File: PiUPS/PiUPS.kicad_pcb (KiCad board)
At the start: 2 copper layers, 87.4 x 56 mm, 92 parts, among them J1 USB_C_Receptacle_USB2.0, J2 Raspberry_Pi_2_3, J3 USB_A, J4 USB_B_Micro, J5 Screw_Terminal_01x02, J6 Screw_Terminal_01x02, Q1 IRF7404, Q2 IRF7404, Q3 IRLML2803TRPBF, Q4 IRF7404, Q5 IRF7404, Q6 IRLML2803TRPBF, Q7 IRLML2803TRPBF, SW1 MODE (JS102011SAQN), SW2 SW_MEC_5E, U1 LM358, U2 BQ25601, U3 TPS61088RHLR, U4 DS3231M

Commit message: beginning of routing
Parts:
- added C26: 100nF, Capacitor_SMD:C_0805_2012Metric_Pad1.18x1.45mm_HandSolder, F.Cu at (313.9, 46.2)
- added C8: 10uF, Capacitor_SMD:C_1206_3216Metric_Pad1.33x1.80mm_HandSolder, F.Cu at (94.2, 109.8)
- added D5: BZV55-B2V4.115, Diode_SMD:D_1206_3216Metric_Pad1.42x1.75mm_HandSolder, F.Cu at (269.0, 84.5)
- added D6: 1PS76SB40.115, Diode_SMD:D_SOD-323_HandSoldering, F.Cu at (268.1, 91.2)
- added Q8: IRF7404, Package_SO:SOIC-8_3.9x4.9mm_P1.27mm, F.Cu at (294.9, 47.9)
- added Q9: IRF7404, Package_SO:SOIC-8_3.9x4.9mm_P1.27mm, F.Cu at (252.2, 104.7)
- added R40: 470, Resistor_SMD:R_0805_2012Metric_Pad1.20x1.40mm_HandSolder, F.Cu at (318.6, 46.2)
- added R41: 470, Resistor_SMD:R_0805_2012Metric_Pad1.20x1.40mm_HandSolder, F.Cu at (250.3, 115.3)
- added R42: 10k, Resistor_SMD:R_0805_2012Metric_Pad1.20x1.40mm_HandSolder, F.Cu at (298.8, 69.4)
- added R43: 0, Resistor_SMD:R_0805_2012Metric_Pad1.20x1.40mm_HandSolder, F.Cu at (250.3, 118.3)
- added R44: 10k, Resistor_SMD:R_0805_2012Metric_Pad1.20x1.40mm_HandSolder, F.Cu at (312.3, 54.1)
- added R45: 470, Resistor_SMD:R_0805_2012Metric_Pad1.20x1.40mm_HandSolder, F.Cu at (306.5, 60.0)
- added R46: 470, Resistor_SMD:R_0805_2012Metric_Pad1.20x1.40mm_HandSolder, F.Cu at (298.8, 66.5)
- added R47: 10k, Resistor_SMD:R_0805_2012Metric_Pad1.20x1.40mm_HandSolder, F.Cu at (270.3, 97.1)
- added R48: 10k, Resistor_SMD:R_0805_2012Metric_Pad1.20x1.40mm_HandSolder, F.Cu at (293.0, 72.4)
- added R49: 10k, Resistor_SMD:R_0805_2012Metric_Pad1.20x1.40mm_HandSolder, F.Cu at (271.5, 94.1)
- added RT1: 10k, Resistor_SMD:R_0603_1608Metric, F.Cu at (110.1, 85.3)
- added U5: FS8205A, Package_SO:TSSOP-8_4.4x3mm_P0.65mm, F.Cu at (252.7, 63.8)
- added U6: DS3231M, Package_SO:SOIC-16W_7.5x10.3mm_P1.27mm, F.Cu at (180.2, 133.0)
- C1: value 47nF -> 20uF; footprint Capacitor_SMD:C_0805_2012Metric_Pad1.18x1.45mm_HandSolder -> Capacitor_SMD:C_1206_3216Metric_Pad1.33x1.80mm_HandSolder
- C10, C19, C24: value 100nF -> 10uF; footprint Capacitor_SMD:C_0805_2012Metric_Pad1.18x1.45mm_HandSolder -> Capacitor_SMD:C_1206_3216Metric_Pad1.33x1.80mm_HandSolder
- C11: value 20uF -> 47nF; footprint Capacitor_SMD:C_1206_3216Metric_Pad1.33x1.80mm_HandSolder -> Capacitor_SMD:C_0805_2012Metric_Pad1.18x1.45mm_HandSolder
- C12, C25, C3: value 10uF -> 100nF; footprint Capacitor_SMD:C_1206_3216Metric_Pad1.33x1.80mm_HandSolder -> Capacitor_SMD:C_0805_2012Metric_Pad1.18x1.45mm_HandSolder
- C13, C15: value 10uF -> 47uF; footprint Capacitor_SMD:C_1206_3216Metric_Pad1.33x1.80mm_HandSolder -> Capacitor_SMD:C_1210_3225Metric_Pad1.33x2.70mm_HandSolder
- C14: value 43pF -> 10uF; footprint Capacitor_SMD:C_0805_2012Metric_Pad1.18x1.45mm_HandSolder -> Capacitor_SMD:C_1206_3216Metric_Pad1.33x1.80mm_HandSolder
- C16: value 8.2nF -> 43pF
- C17: value 1nF -> 47uF; footprint Capacitor_SMD:C_0805_2012Metric_Pad1.18x1.45mm_HandSolder -> Capacitor_SMD:C_1210_3225Metric_Pad1.33x2.70mm_HandSolder
- C18: value 10uF -> 1nF; footprint Capacitor_SMD:C_1206_3216Metric_Pad1.33x1.80mm_HandSolder -> Capacitor_SMD:C_0805_2012Metric_Pad1.18x1.45mm_HandSolder
- C20: value 100nF -> 1000uF; footprint Capacitor_SMD:C_0805_2012Metric_Pad1.18x1.45mm_HandSolder -> Capacitor_SMD:CP_Elec_10x10; moved to F.Cu
- C21: footprint Capacitor_SMD:CP_Elec_10x10 -> Capacitor_SMD:CP_Elec_6.3x7.7
- C23: value 220uF -> 100nF; footprint Capacitor_SMD:CP_Elec_6.3x7.7 -> Capacitor_SMD:C_0805_2012Metric_Pad1.18x1.45mm_HandSolder
- C4: value 10uF -> 20uF
- C5: value 47uF -> 47nF; footprint Capacitor_SMD:C_1210_3225Metric_Pad1.33x2.70mm_HandSolder -> Capacitor_SMD:C_0805_2012Metric_Pad1.18x1.45mm_HandSolder
- C6: value 47uF -> 10uF; footprint Capacitor_SMD:C_1210_3225Metric_Pad1.33x2.70mm_HandSolder -> Capacitor_SMD:C_1206_3216Metric_Pad1.33x1.80mm_HandSolder
- C7: value 47uF -> 100nF; footprint Capacitor_SMD:C_1210_3225Metric_Pad1.33x2.70mm_HandSolder -> Capacitor_SMD:C_0805_2012Metric_Pad1.18x1.45mm_HandSolder
- C9: value 20uF -> 10uF
- D1: value BZV55-B2V4.115 -> 1PS76SB40.115; footprint Diode_SMD:D_1206_3216Metric_Pad1.42x1.75mm_HandSolder -> Diode_SMD:D_SOD-323_HandSoldering; moved to F.Cu
- D2: footprint LED_SMD:LED_0805_2012Metric -> LED_SMD:LED_1206_3216Metric_Pad1.42x1.75mm_HandSolder
- D3: value LED_G -> 1PS76SB40.115; footprint LED_SMD:LED_0805_2012Metric -> Diode_SMD:D_SOD-323_HandSoldering
- D4: value 1N4001 -> 1PS76SB40.115; footprint Diode_SMD:D_1206_3216Metric_Pad1.42x1.75mm_HandSolder -> Diode_SMD:D_SOD-323_HandSoldering; moved to F.Cu
- F1, Q2, Q3, Q4, Q7, R29, R35, R39: moved to F.Cu
- J2: value Raspberry_Pi_2_3 -> USB_B_Micro; footprint RPI:raspberrypi_2_3 -> Connector_USB:USB_Micro-B_Amphenol_10103594-0001LF_Horizontal
- J3: value USB_A -> Screw_Terminal_01x02; footprint Connector_USB:USB_A_Stewart_SS-52100-001_Horizontal -> TerminalBlock:TerminalBlock_Altech_AK300-2_P5.00mm
- J4: value USB_B_Micro -> USB_A; footprint Connector_USB:USB_Micro-B_GCT_USB3076-30-A -> USB:SAMTEC_USB-A-S-X-X-SM2
- J6: value Screw_Terminal_01x02 -> Raspberry_Pi_2_3; footprint TerminalBlock:TerminalBlock_Altech_AK300-2_P5.00mm -> RPI:raspberrypi_2_3
- L2: footprint Inductor_SMD:L_10.4x10.4_H4.8 -> Inductor_SMD:L_6.3x6.3_H3
- Q1, Q5: value IRF7404 -> IRLML2803TRPBF; footprint Package_SO:SOIC-8_3.9x4.9mm_P1.27mm -> IRLML2803TRPBF:SOT95P237X112-3N; moved to F.Cu
- Q6: value IRLML2803TRPBF -> IRF7404; footprint IRLML2803TRPBF:SOT95P237X112-3N -> Package_SO:SOIC-8_3.9x4.9mm_P1.27mm; moved to F.Cu
- R1: value 64.9k -> 10k
- R10: value 10k -> 5.1k; moved to F.Cu
- R11: value 5.1k -> 470
- R12: value 0 -> 470; moved to F.Cu
- R13: value 5.1k -> 10k
- R14: value 100 -> 18k; moved to F.Cu
- R15: value 5.1k -> 200k
- R16: value USR -> 174k
- R17: value USR -> 10k; moved to F.Cu
- R19: value USR -> 1k
- R2, R3, R36, R4: value 10k -> 470; moved to F.Cu
- R20: value USR -> 64.9k
- R21: value USR -> 210k
- R22: value 10k -> 147k; moved to F.Cu
- R23: value 470 -> 100; moved to F.Cu
- R24: value 18.7k -> 470
- R25: value 174k -> 18.7k
- R26: value USR -> 470
- R27: value 147k -> 470
- R28, R31, R33: value 10k -> USR
- R30, R34, R6: value 10k -> USR; moved to F.Cu
- R32: value USR -> 10k
- R37, R38: value 470 -> 10k; moved to F.Cu
- R5: value 210k -> 10k
- R7: value 1k -> 5.1k; moved to F.Cu
- R8: value 1k -> 10k; moved to F.Cu
- SW1: value MODE (JS102011SAQN) -> SW_MEC_5E; footprint Button_Switch_SMD:SW_SPDT_CK-JS102011SAQN -> Button_Switch_SMD:SW_SPST_Omron_B3FS-100xP; moved to F.Cu
- SW2: value SW_MEC_5E -> MODE (JS102011SAQN); footprint Button_Switch_SMD:SW_SPST_Omron_B3FS-100xP -> Button_Switch_SMD:SW_SPDT_CK-JS102011SAQN
- U1: value LM358 -> LM393; moved to F.Cu
- U2: value BQ25601 -> BQ25895RTW
- U4: value DS3231M -> DW01; footprint Package_SO:SOIC-16W_7.5x10.3mm_P1.27mm -> Package_TO_SOT_SMD:SOT-23-6; moved to F.Cu
- moved R15 237.4 mm to (312.8, 49.5), turned to 0 degrees
- moved R32 236.9 mm to (306.1, 63.0), turned to 0 degrees
- moved R14 234.9 mm to (307.5, 54.1)
- moved R28 233.2 mm to (317.5, 52.1), turned to 0 degrees
- moved Q1 226.4 mm to (301.6, 56.7), turned to 0 degrees
- moved D1 225.1 mm to (296.4, 63.5), turned to 0 degrees
- moved R13 222.8 mm to (301.4, 60.4), turned to 0 degrees
- moved R30 222.7 mm to (292.9, 75.3), turned to 0 degrees
- moved R29 215.6 mm to (284.0, 84.6), turned to 0 degrees
- moved U1 215.3 mm to (282.3, 61.9), turned to 0 degrees
- moved Q7 213.8 mm to (307.9, 50.3), turned to 0 degrees
- moved C4 211.9 mm to (282.7, 71.1), turned to 0 degrees
- moved R2 209.4 mm to (279.3, 81.7)
- moved R11 206.3 mm to (283.4, 78.7)
- moved R26 206.1 mm to (311.2, 57.1), turned to 0 degrees
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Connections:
- C1 pad 2: Net-(C1-Pad2) -> GND
- C10 pad 2: GND -> GND1
- C11 pad 1: Net-(C10-Pad1) -> Net-(C11-Pad1)
- C13 pad 1: +BATT -> GND
- C13 pad 2: GND -> VOUT
- C15 pad 1: Net-(C15-Pad1) -> GND
- C15 pad 2: GND -> VOUT
- C17 pad 1: Net-(C17-Pad1) -> GND
- C17 pad 2: GND -> VOUT
- C18 pad 1: GND -> Net-(C18-Pad1)
- C18 pad 2: Net-(C18-Pad2) -> GND
- C19 pad 1: Net-(C19-Pad1) -> +BATT
- C19 pad 2: Net-(C19-Pad2) -> GND
- C2 pad 1: VSYS -> +5V
- C20 pad 1: Net-(C20-Pad1) -> V_UPS
- C20 pad 2: Net-(C20-Pad2) -> GND
- C25 pad 1: V_UPS -> Net-(C25-Pad1)
- C25 pad 2: GND -> Net-(C25-Pad2)
- C3 pad 1: VSYS -> Net-(C1-Pad1)
- C4 pad 1: +5V -> Net-(C1-Pad1)
- C5 pad 1: GND -> Net-(C5-Pad1)
- C5 pad 2: VOUT -> Net-(C5-Pad2)
- C6 pad 1: GND -> GND1
- C6 pad 2: VOUT -> Net-(C6-Pad2)
- C7 pad 1: GND -> Net-(C7-Pad1)
- C7 pad 2: VOUT -> Net-(C7-Pad2)
- C9 pad 1: Net-(C10-Pad1) -> VSYS
- C9 pad 2: GND -> GND1
- D1 pad 2: GND -> +5V
- D2 pad 2: VSYS -> Net-(D2-Pad2)
- D3 pad 2: VSYS -> Net-(D3-Pad2)
- D4 pad 2: +BATT -> Net-(D3-Pad2)
- F1 pad 1: Net-(C10-Pad1) -> Net-(F1-Pad1)
- F2 pad 1: Net-(C10-Pad1) -> Net-(F1-Pad1)
- J1 pad A6: Net-(J1-PadA6) -> unconnected-(J1-PadA6)
- J1 pad A7: Net-(J1-PadA7) -> unconnected-(J1-PadA7)
- J1 pad A8: Net-(J1-PadA8) -> unconnected-(J1-PadA8)
- J1 pad B6: Net-(J1-PadB6) -> unconnected-(J1-PadB6)
- J1 pad B7: Net-(J1-PadB7) -> unconnected-(J1-PadB7)
- J1 pad B8: Net-(J1-PadB8) -> unconnected-(J1-PadB8)
- J2 pad 1: Pi_3v3 -> +5V
- J2 pad 2: V_UPS -> Net-(J2-Pad2)
- J2 pad 3: SDA -> Net-(J2-Pad3)
- J2 pad 4: V_UPS -> unconnected-(J2-Pad4)
- J2 pad 5: SCL -> GND
- J3 pad 1: Net-(F3-Pad2) -> +BATT
- J3 pad 2: Net-(J3-Pad2) -> GND
- J4 pad 1: +5V -> Net-(F3-Pad2)
- J4 pad 4: Net-(J4-Pad4) -> GND
- J6 pad 1: +BATT -> Pi_3v3
- J6 pad 2: GND -> V_UPS
- L1 pad 1: Net-(C1-Pad1) -> Net-(C7-Pad1)
- L1 pad 2: VSYS -> Net-(C1-Pad1)
- L2 pad 1: Net-(C19-Pad1) -> Net-(C5-Pad1)
- L2 pad 2: Net-(C10-Pad1) -> VSYS
- Q1 pad 2: Net-(Q1-Pad1) -> GND
- Q1 pad 3: Net-(Q1-Pad1) -> Net-(Q1-Pad3)
- Q2 pad 1: Net-(Q1-Pad1) -> Net-(F1-Pad1)
- Q2 pad 2: Net-(Q1-Pad1) -> Net-(F1-Pad1)
- Q2 pad 3: Net-(Q1-Pad1) -> Net-(F1-Pad1)
- Q2 pad 4: Net-(Q1-Pad4) -> Net-(Q1-Pad3)
- Q2 pad 5: V_UPS -> Net-(C1-Pad1)
- Q2 pad 6: V_UPS -> Net-(C1-Pad1)
- Q2 pad 7: V_UPS -> Net-(C1-Pad1)
- Q2 pad 8: V_UPS -> Net-(C1-Pad1)
- Q3 pad 1: Net-(Q3-Pad1) -> Net-(C25-Pad1)
- Q4 pad 1: Net-(C20-Pad1) -> Net-(Q4-Pad1)
- Q4 pad 2: Net-(C20-Pad1) -> Net-(Q4-Pad1)
- Q4 pad 3: Net-(C20-Pad1) -> Net-(Q4-Pad1)
- Q4 pad 4: Net-(C20-Pad2) -> Net-(Q4-Pad4)
- Q4 pad 5: VOUT -> +5V
- Q4 pad 6: VOUT -> +5V
- Q4 pad 7: VOUT -> +5V
- Q4 pad 8: VOUT -> +5V
- Q5 pad 1: Net-(C20-Pad1) -> Net-(Q5-Pad1)
- Q5 pad 2: Net-(C20-Pad1) -> GND
- Q5 pad 3: Net-(C20-Pad1) -> Net-(Q5-Pad3)
- Q6 pad 1: Net-(Q6-Pad1) -> Net-(C26-Pad1)
- Q6 pad 2: GND -> Net-(C26-Pad1)
- Q6 pad 3: Net-(Q6-Pad3) -> Net-(C26-Pad1)
- R1 pad 1: Net-(R1-Pad1) -> GND
- R1 pad 2: GND -> Net-(R1-Pad2)
- R10 pad 1: INT -> Net-(J1-PadA5)
- R10 pad 2: Pi_3v3 -> GND
- R11 pad 1: Net-(J1-PadB5) -> Net-(R11-Pad1)
- R11 pad 2: GND -> Net-(R11-Pad2)
- R12 pad 1: Net-(J2-Pad7) -> Net-(R11-Pad2)
- R12 pad 2: INT -> GND1
- R13 pad 1: Net-(D2-Pad1) -> GND1
- R14 pad 1: Net-(Q3-Pad3) -> Net-(R14-Pad1)
- R14 pad 2: Net-(Q1-Pad4) -> Net-(C1-Pad1)
- R15 pad 1: Net-(D3-Pad1) -> GND
- R15 pad 2: Net-(R15-Pad2) -> Net-(R14-Pad1)
- R16 pad 1: Net-(J3-Pad3) -> Net-(C7-Pad1)
- R16 pad 2: V_UPS -> Net-(R16-Pad2)
- R17 pad 1: Net-(D4-Pad1) -> Net-(R17-Pad1)
- R17 pad 2: +BATT -> Net-(C6-Pad2)
- R18 pad 1: Net-(R18-Pad1) -> GND1
- R18 pad 2: GND -> Net-(R17-Pad1)
- R19 pad 1: GND -> GND1
- R19 pad 2: Net-(J3-Pad3) -> Net-(R19-Pad2)
- R2 pad 2: +5V -> Net-(R2-Pad2)
- R20 pad 1: Net-(J3-Pad3) -> Net-(R20-Pad1)
- R20 pad 2: Net-(J3-Pad2) -> GND
- R21 pad 1: Net-(J3-Pad2) -> VOUT
- R21 pad 2: V_UPS -> Net-(R20-Pad1)
- R22 pad 1: Net-(R22-Pad1) -> GND
- R22 pad 2: VSYS -> Net-(R22-Pad2)
- R23 pad 1: Net-(R23-Pad1) -> +BATT
- R23 pad 2: Net-(Q3-Pad1) -> Net-(C12-Pad1)
- R24 pad 1: Net-(C17-Pad1) -> Net-(D3-Pad2)
- R24 pad 2: Net-(C14-Pad1) -> +5V
- R25 pad 1: Net-(C19-Pad1) -> Net-(C18-Pad1)
- R25 pad 2: Net-(R25-Pad2) -> Net-(C16-Pad1)
- R26 pad 1: GND -> 2V4
- R26 pad 2: Net-(J3-Pad2) -> VOUT
- R27 pad 1: GND -> 2V4
- R27 pad 2: Net-(R27-Pad2) -> VOUT
- R28 pad 1: Net-(R28-Pad1) -> Net-(J4-Pad3)
- R28 pad 2: Net-(C15-Pad1) -> Net-(J4-Pad2)
- R29 pad 1: GND -> Net-(C25-Pad2)
- R29 pad 2: Net-(R22-Pad1) -> GND
- R3 pad 1: Net-(R2-Pad1) -> Net-(D1-Pad1)
- R3 pad 2: GND -> Net-(R2-Pad1)
- R30 pad 1: Net-(Q3-Pad1) -> Net-(J4-Pad3)
- R30 pad 2: GND -> V_UPS
- R31 pad 2: Net-(R28-Pad1) -> Net-(J4-Pad2)
- R32 pad 1: Net-(J4-Pad3) -> Net-(C25-Pad2)
- R32 pad 2: Net-(J4-Pad2) -> +5V
- R33 pad 1: Net-(R33-Pad1) -> GND
- R33 pad 2: VSYS -> Net-(J4-Pad3)
- R34 pad 1: Net-(C20-Pad2) -> Net-(J4-Pad2)
- R34 pad 2: Net-(C20-Pad1) -> V_UPS
- R35 pad 1: Net-(Q6-Pad3) -> Net-(R35-Pad1)
- R35 pad 2: Net-(C20-Pad2) -> VOUT
- R36 pad 1: Net-(Q6-Pad1) -> Net-(R35-Pad1)
- R36 pad 2: VOUT -> Net-(C25-Pad1)
- R37 pad 1: Net-(Q7-Pad3) -> GND
- R37 pad 2: Net-(Q6-Pad1) -> Net-(C25-Pad1)
- R38 pad 1: Net-(R23-Pad1) -> Net-(Q7-Pad1)
- R38 pad 2: Net-(Q7-Pad1) -> VOUT
- R39 pad 1: GND -> SDA
- R39 pad 2: Net-(Q7-Pad1) -> Pi_3v3
- R4 pad 1: SDA -> Net-(R4-Pad1)
- R4 pad 2: Pi_3v3 -> Net-(R2-Pad1)
- R5 pad 1: VOUT -> Net-(F1-Pad1)
- R5 pad 2: Net-(R1-Pad1) -> Net-(Q1-Pad3)
- R6 pad 1: SCL -> Net-(J2-Pad3)
- R6 pad 2: Pi_3v3 -> Net-(J2-Pad2)
- R7 pad 1: Net-(D1-Pad1) -> Net-(J1-PadB5)
- R7 pad 2: VSYS -> GND
- R8 pad 1: Net-(Q1-Pad4) -> Net-(R2-Pad1)
- R8 pad 2: Net-(Q1-Pad1) -> Net-(C1-Pad1)
- R9 pad 1: Net-(J1-PadA5) -> VSYS
- R9 pad 2: GND -> Net-(D2-Pad2)
- SW1 pad 1: VSYS -> +BATT
- SW1 pad 2: Net-(SW1-Pad2) -> +BATT
- SW1 pad 3: GND -> Net-(R2-Pad2)
- SW2 pad 1: GND -> Net-(R2-Pad1)
- SW2 pad 2: GND -> Net-(Q1-Pad1)
- SW2 pad 3: Net-(SW2-Pad3) -> Net-(R1-Pad2)
- U1 pad 1: Net-(R23-Pad1) -> Net-(R35-Pad1)
- U1 pad 2: Net-(D1-Pad1) -> 2V4
- U1 pad 3: Net-(R2-Pad1) -> Net-(C25-Pad2)
- U1 pad 5: Net-(R22-Pad1) -> Net-(R14-Pad1)
- U1 pad 6: Net-(U1-Pad6) -> 2V4
- U1 pad 7: Net-(U1-Pad6) -> Net-(R4-Pad1)
- U1 pad 8: VSYS -> VOUT
- U2 pad 10: Net-(U2-Pad10) -> Net-(R11-Pad1)
- U2 pad 11: Net-(R28-Pad1) -> Net-(R17-Pad1)
- U2 pad 12: Net-(SW2-Pad3) -> unconnected-(U2-Pad12)
- U2 pad 17: GND -> GND1
- U2 pad 18: GND -> GND1
- U2 pad 19: Net-(C1-Pad1) -> Net-(C5-Pad1)
- U2 pad 2: Net-(R33-Pad1) -> Net-(U2-Pad2)
- U2 pad 20: Net-(C1-Pad1) -> Net-(C5-Pad1)
- U2 pad 21: Net-(C1-Pad2) -> Net-(C5-Pad2)
- U2 pad 22: Net-(C15-Pad1) -> Net-(C6-Pad2)
- U2 pad 23: Net-(C18-Pad2) -> Net-(C10-Pad1)
- U2 pad 24: +5V -> unconnected-(U2-Pad24)
- U2 pad 25: GND -> GND1
- U2 pad 3: Net-(R15-Pad2) -> Net-(U2-Pad2)
- U2 pad 4: Net-(R13-Pad2) -> Net-(D2-Pad1)
- U2 pad 8: Net-(U2-Pad8) -> GND1
- U2 pad 9: Net-(R18-Pad1) -> Net-(R13-Pad2)
- U3 pad 1: Net-(C12-Pad1) -> Net-(C14-Pad1)
- U3 pad 10: Net-(C16-Pad1) -> Net-(C11-Pad1)
- U3 pad 11: GND -> unconnected-(U3-Pad11)
- U3 pad 12: GND -> unconnected-(U3-Pad12)
- U3 pad 13: Net-(U3-Pad13) -> unconnected-(U3-Pad13)
- U3 pad 17: Net-(R1-Pad1) -> Net-(R20-Pad1)
- U3 pad 18: Net-(C14-Pad1) -> Net-(C16-Pad1)
- U3 pad 19: Net-(R27-Pad2) -> Net-(R22-Pad2)
- U3 pad 2: Net-(SW1-Pad2) -> VSYS
- U3 pad 3: Net-(R25-Pad2) -> Net-(R16-Pad2)
- U3 pad 4: Net-(C19-Pad1) -> Net-(C7-Pad1)
- U3 pad 5: Net-(C19-Pad1) -> Net-(C7-Pad1)
- U3 pad 6: Net-(C19-Pad1) -> Net-(C7-Pad1)
- U3 pad 7: Net-(C19-Pad1) -> Net-(C7-Pad1)
- U3 pad 8: Net-(C19-Pad2) -> Net-(C7-Pad2)
- U3 pad 9: Net-(C10-Pad1) -> Net-(C1-Pad1)
- U4 pad 1: Net-(U4-Pad1) -> Net-(D4-Pad1)
- U4 pad 2: Pi_3v3 -> Net-(R19-Pad2)
- U4 pad 3: Net-(U4-Pad3) -> Net-(D3-Pad1)
- U4 pad 4: Net-(U4-Pad4) -> unconnected-(U4-Pad4)
- U4 pad 5: GND -> Net-(C12-Pad1)
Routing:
- net VSYS: track 113.8 -> 0.00 mm, vias 3 -> 0
- net SDA: track 114.6 -> 1.52 mm, vias 3 -> 1
- net Net-(R23-Pad1): track 105.5 -> 0.00 mm, vias 4 -> 0
- net SCL: track 104.3 -> 1.86 mm, vias 3 -> 1
- net V_UPS: track 95.2 -> 0.00 mm, vias 48 -> 0
- net INT: track 89.3 -> 1.47 mm, vias 3 -> 1
- net Pi_3v3: track 72.8 -> 0.00 mm, vias 2 -> 0
- net GND: track 67.2 -> 0.00 mm, vias 19 -> 0
- net Net-(SW2-Pad3): track 47.6 -> 0.00 mm, vias 2 -> 0
- net Net-(SW1-Pad2): track 35.1 -> 0.00 mm, vias 1 -> 0
- net Net-(C15-Pad1): track 35.1 -> 0.00 mm, vias 2 -> 0
- net Net-(R33-Pad1): track 21.6 -> 0.00 mm
- net +BATT: track 17.0 -> 0.00 mm, vias 20 -> 0
- net VOUT: track 16.6 -> 0.00 mm, vias 9 -> 0
- net +5V: track 37.0 -> 22.2 mm, vias 6 -> 0
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- added copper zone on F.Cu, net Net-(C5-Pad1)
- removed copper zone on B.Cu, net +5V
- removed copper zone on F.Cu, net +5V
- removed copper zone on B.Cu, net +BATT
- removed copper zone on F.Cu, net +BATT
- removed copper zone on B.Cu, net GND
- removed copper zone on F.Cu, net GND
- removed copper zone on F.Cu, net Net-(C1-Pad1)
- removed copper zone on B.Cu, net Net-(C10-Pad1)
- removed copper zone on F.Cu, net Net-(C10-Pad1)
- removed copper zone on F.Cu, net Net-(C19-Pad1)
- removed copper zone on B.Cu, net Net-(C20-Pad1)
- removed copper zone on B.Cu, net Net-(Q1-Pad1)
- removed copper zone on B.Cu, net VOUT
- removed copper zone on F.Cu, net VOUT
- removed copper zone on F.Cu, net VSYS
- removed copper zone on B.Cu, net V_UPS
- removed copper zone on F.Cu, net V_UPS
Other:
- board text removed: "+"
- board text removed: "18650 BATT"
- board text removed: "5VIN"
- board text removed: "BAT EN"
- board text removed: "DDL PI UPS rev 0.2"
- board text removed: "EXT BATT"
- board text removed: "OUTDATED PCB"
- board text removed: "Place a shunt or a diode to enable RTC (see RTC notes)"
- board text removed: "Place a shunt to enable interrupt from battery management chip"
- board text removed: "Select USB port or screw terminal"
- board text removed: "Select resistors to suit your load (see USB notes)"
- board text removed: "UPS OFF ON"
- board text removed: "UPS VOUT"
- board text removed: "dmytroengineering.com/piups"

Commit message: Continued routing
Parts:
- C8: value 10uF -> 100nF; footprint Capacitor_SMD:C_1206_3216Metric_Pad1.33x1.80mm_HandSolder -> Capacitor_SMD:C_0805_2012Metric_Pad1.18x1.45mm_HandSolder
- R21: renamed from R6; moved to B.Cu
- R6: renamed from R10; moved to B.Cu
- R7: moved to B.Cu
- moved R21 252.1 mm to (73.3, 111.6), turned to 90 degrees
- moved R18 222.5 mm to (86.1, 116.9), turned to 180 degrees
- moved R9 200.6 mm to (86.1, 115.0)
- moved U3 196.7 mm to (107.7, 115.4)
- moved R6 187.0 mm to (77.5, 120.1), turned to -90 degrees
- moved R7 178.8 mm to (80.5, 120.2), turned to -90 degrees
- moved R12 161.3 mm to (89.0, 115.9), turned to -90 degrees
- moved U4 161.3 mm to (101.4, 119.8)
- moved C8 22.4 mm to (116.3, 106.5)
- moved R14 6.26 mm to (91.4, 118.0)
- moved C3 5.56 mm to (92.9, 105.4), turned to 90 degrees
- moved R19 3.53 mm to (88.5, 118.9)
- renumbered C2 to C1, C15 to C10, C17 to C11, C20 to C12, C21 to C13, C22 to C14, C23 to C15, C24 to C16, C25 to C17, C1 to C18, C3 to C19, C5 to C2, C4 to C20, C14 to C21, C16 to C22, C11 to C23, C18 to C24, C7 to C25, C9 to C3, C10 to C4, C12 to C5, C19 to C6, C6 to C7, C26 to C8, C13 to C9, D5 to D1, D3 to D2, D4 to D3, D2 to D4, D1 to D5, J6 to J4, J4 to J5, J5 to J6, L2 to L1, L1 to L2, Q4 to Q1, Q8 to Q2, Q5 to Q3, Q6 to Q4, Q9 to Q5, Q7 to Q6, Q3 to Q7, Q2 to Q8, Q1 to Q9, R32 to R1, R45 to R10, R23 to R11, R41 to R13, R17 to R14, R19 to R15, R24 to R16, R9 to R17, R13 to R18, R18 to R19, R29 to R2, R44 to R20, R49 to R22, R46 to R23, R38 to R24, R40 to R25, R20 to R26, R36 to R27, R21 to R28, R37 to R29, R26 to R3, R5 to R30, R1 to R31, R25 to R32, R16 to R33, R22 to R34, R2 to R35, R3 to R36, R8 to R37, R4 to R38, R14 to R39, R27 to R4, R39 to R40, R15 to R41, R47 to R43, R43 to R44, R30 to R45, R33 to R46, R28 to R47, R34 to R48, R31 to R49, R48 to R5, R35 to R8, R11 to R9, U4 to U3, U5 to U4, U3 to U5
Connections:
- C8 pad 1: Net-(C26-Pad1) -> Net-(C8-Pad1)
- C8 pad 2: Net-(C26-Pad2) -> Net-(C8-Pad2)
- C8 pad 1: VSYS -> Net-(C8-Pad1)
- C8 pad 2: GND1 -> Net-(C8-Pad2)
- Q4 pad 1: Net-(C26-Pad1) -> Net-(C8-Pad1)
- Q4 pad 2: Net-(C26-Pad1) -> Net-(C8-Pad1)
- Q4 pad 3: Net-(C26-Pad1) -> Net-(C8-Pad1)
- Q4 pad 4: Net-(C26-Pad2) -> Net-(C8-Pad2)
- Q5 pad 1: Net-(C26-Pad1) -> Net-(C8-Pad1)
- Q5 pad 2: Net-(C26-Pad1) -> Net-(C8-Pad1)
- Q5 pad 3: Net-(C26-Pad1) -> Net-(C8-Pad1)
- Q5 pad 4: Net-(C26-Pad2) -> Net-(C8-Pad2)
- R22 pad 1: Net-(C26-Pad2) -> Net-(C8-Pad2)
- R22 pad 2: Net-(C26-Pad1) -> Net-(C8-Pad1)
- R23 pad 2: Net-(C26-Pad2) -> Net-(C8-Pad2)
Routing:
- net Net-(R14-Pad1): track 0.00 -> 59.7 mm, vias 0 -> 2
- net GND1: track 0.00 -> 26.3 mm
- net Net-(C7-Pad2): track 2.04 -> 24.1 mm, vias 0 -> 2
- net Net-(R18-Pad2): track 0.00 -> 6.12 mm
- net Net-(J2-Pad2): track 0.00 -> 5.90 mm, vias 0 -> 1
- net Net-(J2-Pad3): track 0.00 -> 5.51 mm, vias 0 -> 1
- net Net-(R9-Pad1): track 0.00 -> 4.69 mm
- net Net-(J1-PadA5): track 0.00 -> 2.67 mm, vias 0 -> 1
- net Net-(J1-PadB5): track 0.00 -> 2.59 mm, vias 0 -> 1
- net +5V: track 22.2 -> 24.0 mm
- net +BATT: vias 0 -> 6
- added copper zone on B.Cu, net +BATT
- added copper zone on F.Cu, net +BATT
- added copper zone on F.Cu, net GND1
- added copper zone on F.Cu, net VSYS

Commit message: continued routing
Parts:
- moved R16 217.9 mm to (95.7, 112.3), turned to 90 degrees
- moved R3 214.8 mm to (101.9, 105.1)
- moved R4 207.5 mm to (98.1, 105.1), turned to 180 degrees
- moved R15 204.8 mm to (95.6, 119.7), turned to -90 degrees
- moved D5 200.9 mm to (101.9, 113.7), turned to 180 degrees
- moved R8 193.0 mm to (95.2, 106.0), turned to 90 degrees
- moved R30 191.8 mm to (106.1, 104.6), turned to 180 degrees
- moved U1 187.9 mm to (100.4, 108.8)
- moved C5 183.7 mm to (98.8, 116.1), turned to 90 degrees
- moved R11 183.5 mm to (92.3, 122.2), turned to 180 degrees
- moved R38 181.3 mm to (100.8, 117.0), turned to -90 degrees
- moved F2 176.7 mm to (97.4, 102.0), turned to 180 degrees
- moved C20 175.7 mm to (109.2, 98.6), turned to 90 degrees
- moved R35 175.1 mm to (107.5, 115.7)
- moved C10 174.4 mm to (114.4, 113.2)
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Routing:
- net +5V: track 24.0 -> 61.4 mm, vias 0 -> 11
- net GND1: track 26.3 -> 57.5 mm, vias 0 -> 11
- net +BATT: track 0.00 -> 27.5 mm, vias 6 -> 8
- net VSYS: track 0.00 -> 26.6 mm, vias 0 -> 3
- net Net-(R13-Pad1): track 0.00 -> 22.7 mm
- net Net-(C18-Pad1): track 0.00 -> 18.5 mm, vias 0 -> 2
- net VOUT: track 0.00 -> 17.9 mm, vias 0 -> 2
- net Net-(D3-Pad1): track 0.00 -> 16.1 mm, vias 0 -> 2
- net Net-(D5-Pad1): track 0.00 -> 15.1 mm, vias 0 -> 2
- net 2V4: track 0.00 -> 14.7 mm
- net Net-(C5-Pad1): track 0.00 -> 12.9 mm, vias 0 -> 2
- net Net-(D2-Pad1): track 0.00 -> 10.2 mm
- net Net-(R35-Pad1): track 0.00 -> 9.92 mm
- net Net-(R38-Pad1): track 0.00 -> 9.81 mm, vias 0 -> 2
- net Net-(C25-Pad1): track 0.00 -> 9.32 mm
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- added copper zone on F.Cu, net +5V
- added copper zone on B.Cu, net GND1
- added copper zone on F.Cu, net Net-(C18-Pad1)
- added copper zone on F.Cu, net Net-(C25-Pad1)
- added copper zone on F.Cu, net Net-(F1-Pad1)
- added copper zone on F.Cu, net VOUT

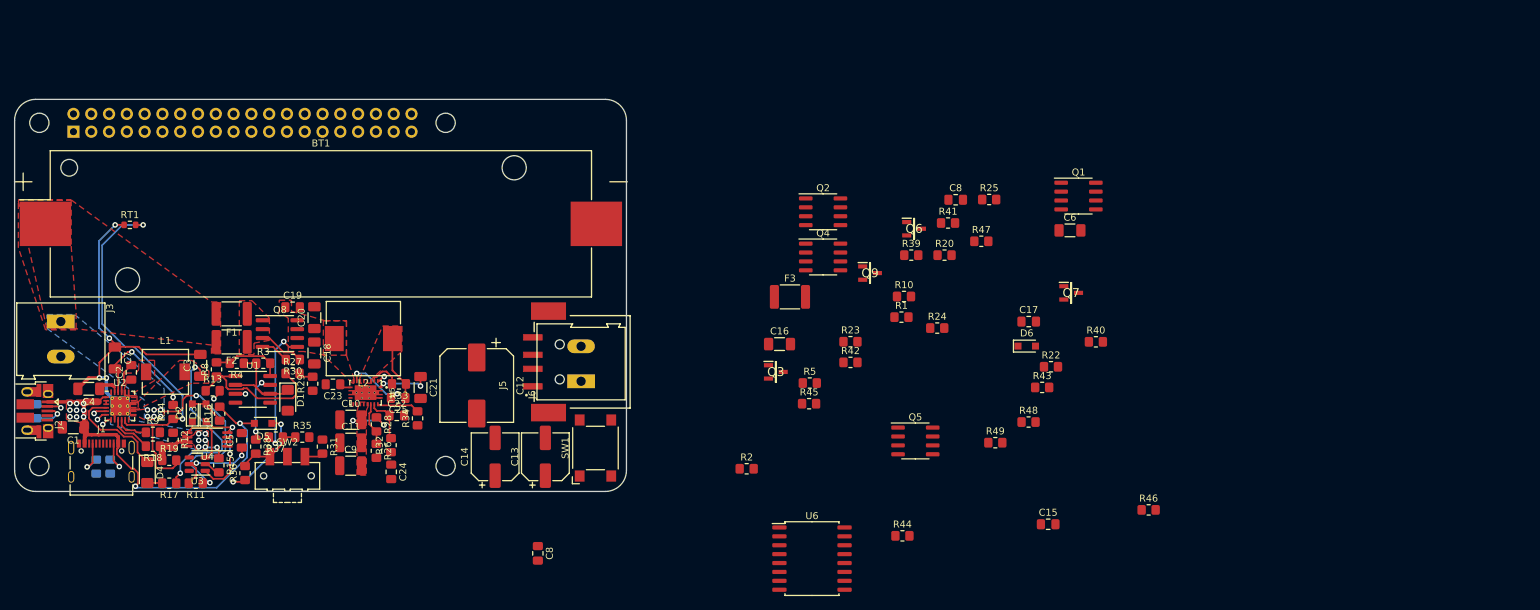
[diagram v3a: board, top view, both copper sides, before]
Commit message: almost finished routing
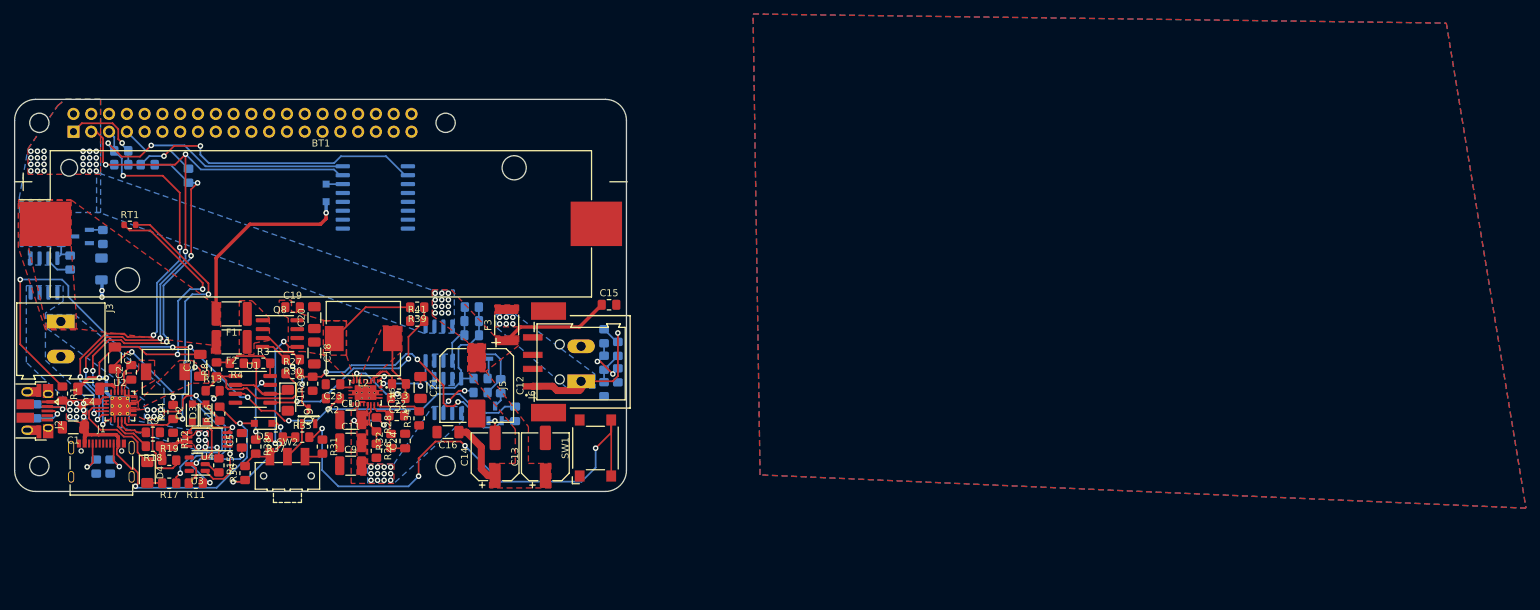
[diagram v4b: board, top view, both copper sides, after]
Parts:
- C17, C6, C8 (x2), D6, Q1, Q2, Q3, Q4, Q5, Q6, Q7, R10, R20, R22, R23, R24, R25, R40, R42, R43, R44, R45, R46, R47, R48, R49, R5, U6: moved to B.Cu
- moved Q1 148.1 mm to (70.6, 92.6), turned to -90 degrees
- moved R40 141.4 mm to (81.6, 76.8)
- moved C6 138.4 mm to (78.8, 91.6), turned to 90 degrees
- moved R43 131.6 mm to (85.4, 76.8), turned to 180 degrees
- moved R10 120.6 mm to (73.0, 86.9), turned to -90 degrees
- moved R1 120.3 mm to (73.2, 109.4), turned to -90 degrees
- moved R20 120.2 mm to (79.0, 87.1), turned to -90 degrees
- moved R44 114.2 mm to (91.2, 78.3), turned to -90 degrees
- moved Q2 112.5 mm to (69.3, 85.1), turned to 90 degrees
- moved R42 108.4 mm to (81.6, 74.8)
- moved R5 107.0 mm to (74.3, 90.7), turned to -90 degrees
- moved D6 102.4 mm to (110.9, 80.8), turned to -90 degrees
- moved Q3 100.9 mm to (76.0, 87.0), turned to 180 degrees
- moved Q7 84.0 mm to (135.0, 112.2), turned to 90 degrees
- moved R22 83.1 mm to (131.7, 97.1), turned to 180 degrees
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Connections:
- R45 pad 2: V_UPS -> Net-(F3-Pad2)
- R48 pad 2: V_UPS -> Net-(F3-Pad2)
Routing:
- net Net-(C17-Pad2): track 1.43 -> 105.0 mm, vias 1 -> 6
- net SCL: track 1.86 -> 98.5 mm, vias 1 -> 7
- net SDA: track 1.52 -> 94.1 mm, vias 1 -> 6
- net Net-(R35-Pad2): track 0.00 -> 71.3 mm, vias 0 -> 4
- net Pi_3v3: track 0.00 -> 57.2 mm, vias 0 -> 3
- net INT: track 1.47 -> 55.7 mm, vias 1 -> 5
- net Net-(C17-Pad1): track 2.07 -> 39.6 mm, vias 0 -> 3
- net +BATT: track 27.5 -> 58.2 mm, vias 8 -> 11
- net Net-(R39-Pad1): track 0.00 -> 30.6 mm, vias 0 -> 2
- net V_UPS: track 0.00 -> 25.3 mm, vias 0 -> 36
- net Net-(F3-Pad2): track 0.00 -> 24.1 mm, vias 0 -> 7
- net Net-(C8-Pad2): track 0.00 -> 23.2 mm
- net Net-(C18-Pad1): track 18.5 -> 31.2 mm
- net Net-(J4-Pad7): track 0.00 -> 11.0 mm
- net Net-(Q1-Pad4): track 0.00 -> 11.0 mm
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- added copper zone on B.Cu, net +5V
- added copper zone on B.Cu, net GND
- added copper zone on F.Cu, net GND
- added copper zone on B.Cu, net Net-(C8-Pad1)
- added copper zone on B.Cu, net Net-(F3-Pad2)
- added copper zone on F.Cu, net Net-(F3-Pad2)
- added copper zone on B.Cu, net Net-(Q1-Pad1)
- added copper zone on B.Cu, net VOUT
- added copper zone on B.Cu, net V_UPS
- added copper zone on F.Cu, net V_UPS
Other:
- board text added: "Set all zones to priority 1"

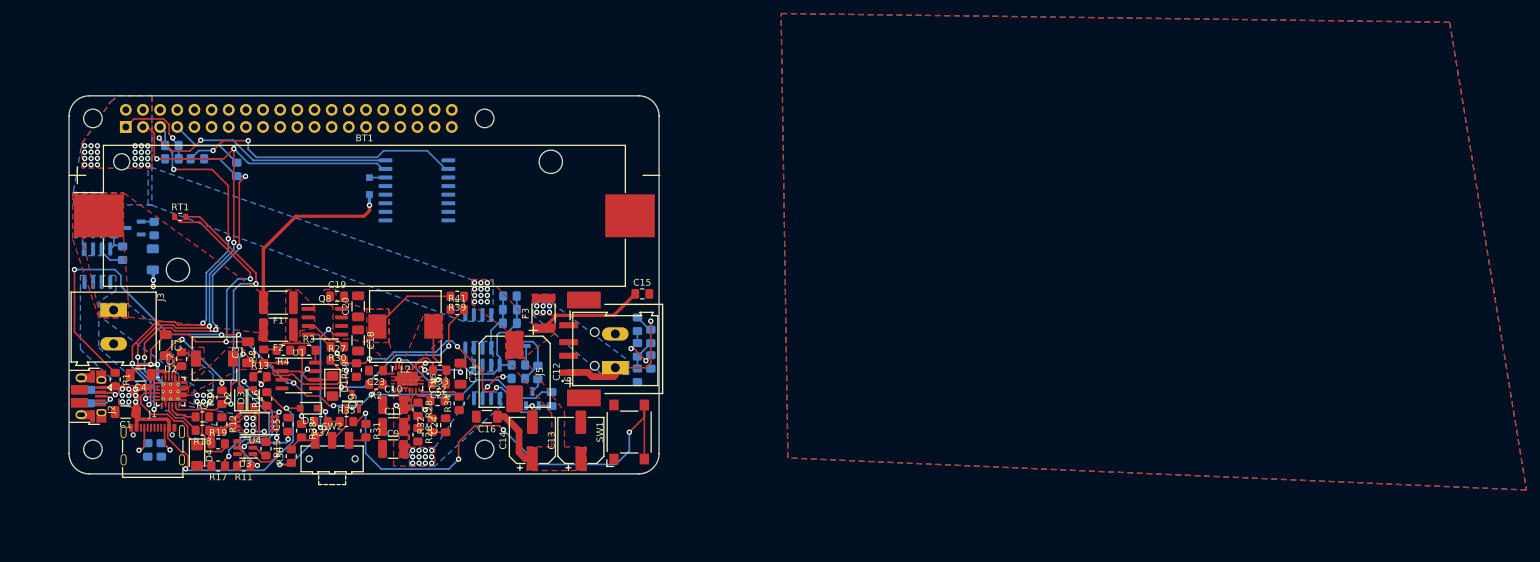
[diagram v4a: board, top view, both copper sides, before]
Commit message: finshed layout and routing
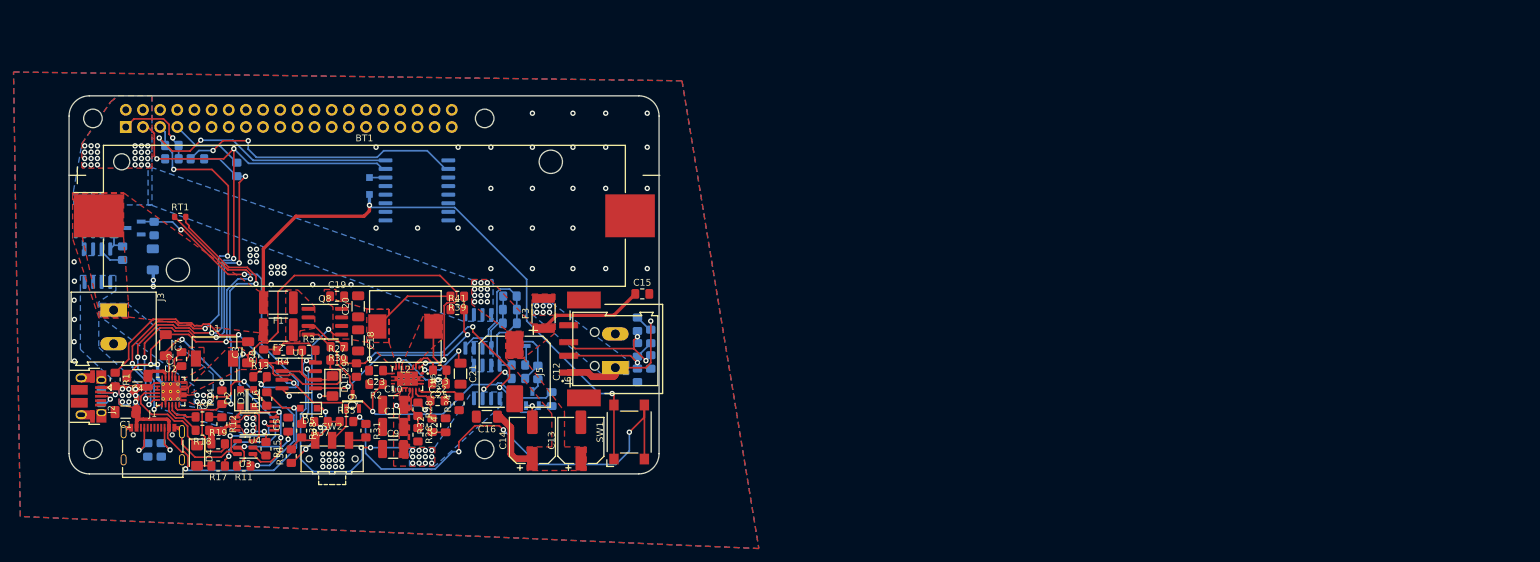
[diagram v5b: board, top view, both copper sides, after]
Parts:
- moved R21 1.63 mm to (71.2, 111.9)
- moved C4 0.49 mm to (76.5, 108.9)
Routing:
- net +BATT: track 58.2 -> 119.9 mm, vias 11 -> 12
- net VSYS: track 26.4 -> 83.7 mm, vias 3 -> 4
- net Net-(Q3-Pad1): track 3.43 -> 46.6 mm, vias 1 -> 3
- net VOUT: track 23.9 -> 61.6 mm, vias 16 -> 19
- net GND: track 5.01 -> 34.4 mm, vias 1 -> 65
- net Net-(C17-Pad2): track 105.0 -> 85.3 mm, vias 6 -> 3
- net Net-(J5-Pad2): track 4.57 -> 15.2 mm, vias 0 -> 1
- net Net-(J5-Pad3): track 7.12 -> 17.4 mm
- net Net-(C8-Pad2): track 23.2 -> 28.9 mm
- net Net-(C17-Pad1): track 39.6 -> 43.5 mm
- net Net-(D5-Pad1): track 14.8 -> 11.2 mm
- net INT: track 55.7 -> 58.3 mm
- net SDA: track 94.1 -> 96.6 mm
- net Net-(R35-Pad2): track 71.3 -> 69.4 mm
- net Net-(R12-Pad1): track 0.00 -> 1.91 mm
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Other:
- board text removed: "Set all zones to priority 1"

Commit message: silkscreen orginization
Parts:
- removed the C8 at (131.7, 101.1)
- added G***: LOGO, logo:warning, F.Cu at (88.4, 85.1)
- added G***: LOGO, logo:warning, F.Cu at (129.8, 85.1)
- moved R22 3.51 mm to (130.7, 100.5), turned to -90 degrees
- moved C8 2.81 mm to (130.2, 96.6), turned to -90 degrees
- moved R14 0.18 mm to (89.0, 112.2)
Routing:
- net Net-(C8-Pad2): track 28.9 -> 12.0 mm
- net Net-(C8-Pad1): track 8.84 -> 10.9 mm
- net Net-(F3-Pad2): track 24.1 -> 25.7 mm
- net +BATT: track 119.9 -> 121.4 mm
- net GND: vias 65 -> 87
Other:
- board text added: "CHECK BATTERY POLARITY"
